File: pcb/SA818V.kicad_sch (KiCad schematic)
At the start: 7 parts, among them J12 RF_SMA, Q11 BSS138, Q12 BSS138, U19 SA818S-V

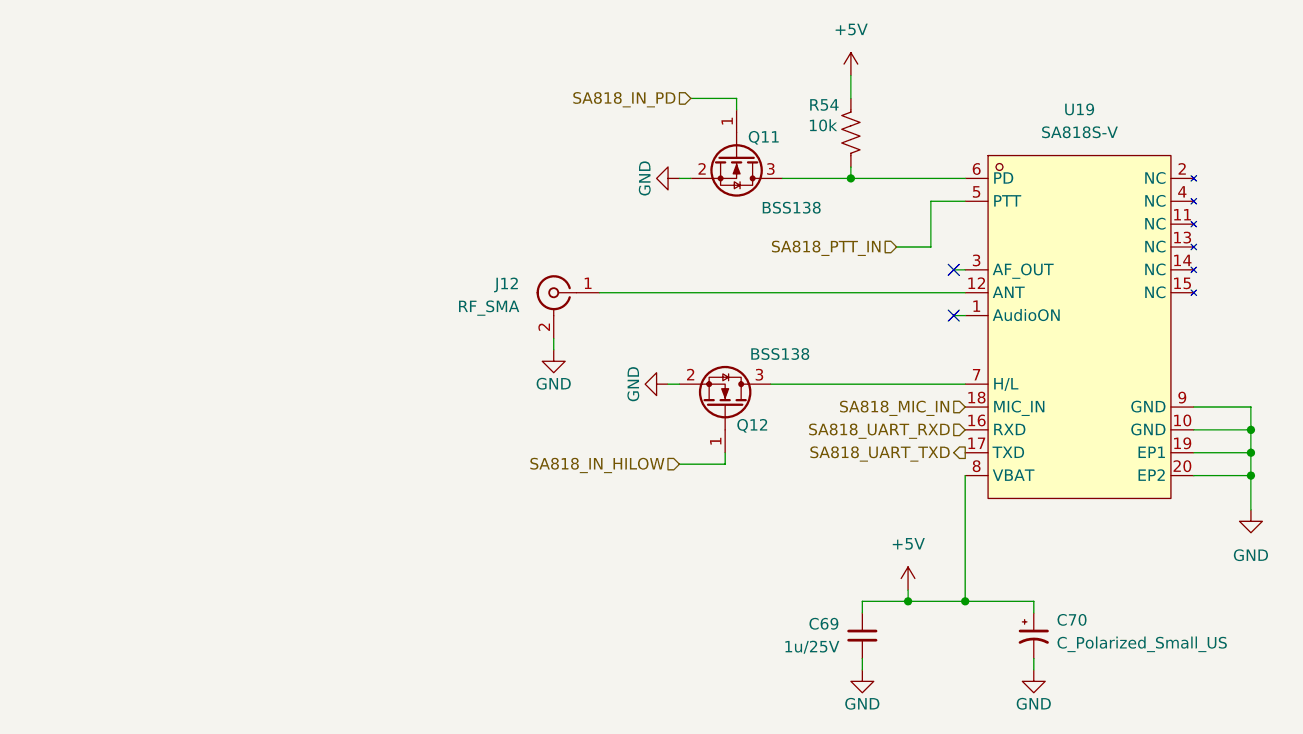
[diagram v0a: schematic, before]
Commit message: Wire SA818 PD/H-L and PTT opto, GPS power gating with bench bypass, RF detector groundwork
- SA818S-V: wire PD/H-L to PCA9555 expander outputs; swap PTT-keying FET
  for PC817 optocoupler isolation on the shared SA818S/external-HT PTT line
- GPS: add Q10 (AO3407A) high-side P-FET gating VCC+VCC_IO together for
  genuine hardware backup mode, driven via Q13 level-shifter from a new
  PCA9555 output (PERIPH_OUT_GPS_PWRON); add JP28 as a source-to-drain
  bench bypass across Q10 for unconditional power during bring-up; wire
  EXTINT to another PCA9555 output (PERIPH_OUT_GPS_EXTINT, pulled low by
  R57) to experiment with UART software-standby + external wake
- peripherals: reassign PCA9555 channels for the above plus SA818 PD/H-L
- audio/mcu-esp32: forward-power detector tap wiring groundwork
- docs: add vhf_matching_detector.md (matching network + RF detector BOM
  and layout), index it in _docs/README.md

Co-Authored-By: Claude Sonnet 5 <noreply@anthropic.com>
Claude-Session: https://claude.ai/code/session_01LhLkuH6sQ5GbUZ61bG7p2h
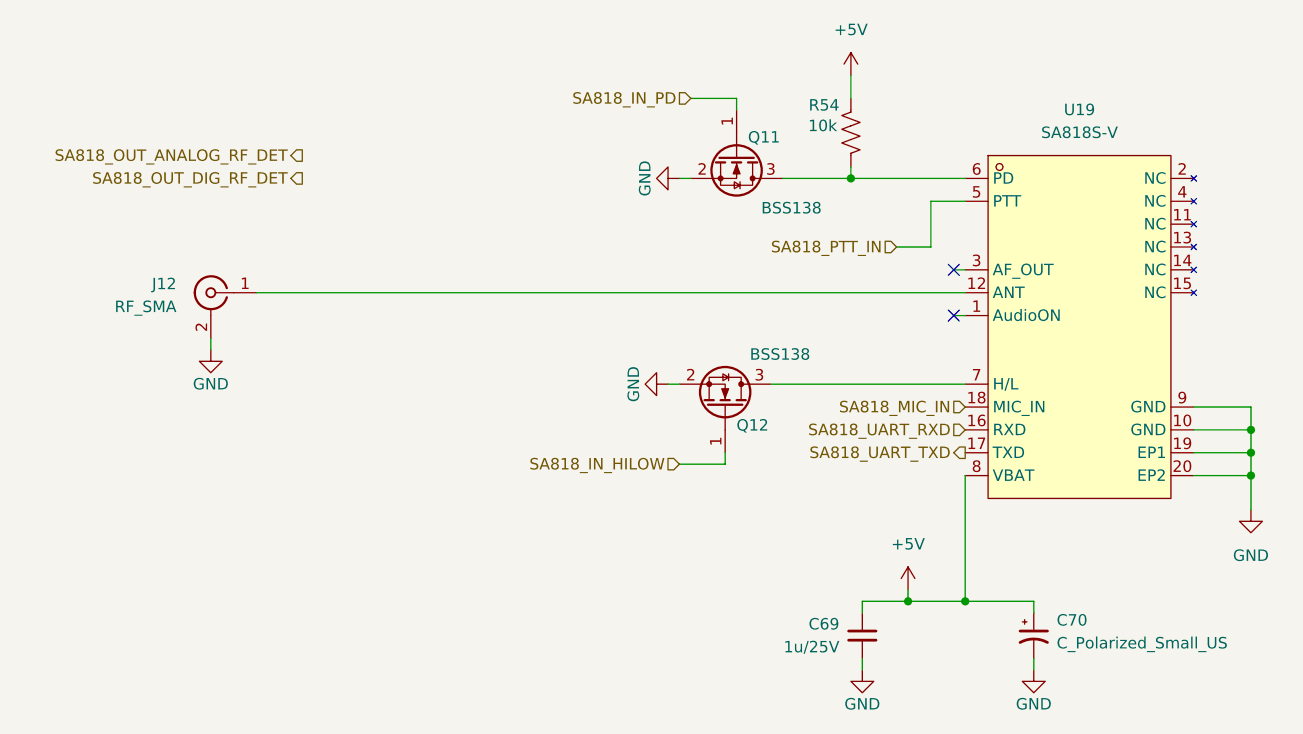
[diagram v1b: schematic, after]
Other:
- moved on the sheet: J12
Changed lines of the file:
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@@
 	(wire
 		(pts
-			(xy 82.55 80.01) (xy 82.55 81.28)
+			(xy 44.45 80.01) (xy 44.45 81.28)
 		)
 		(stroke
@@
 	(wire
 		(pts
-			(xy 87.63 74.93) (xy 128.27 74.93)
+			(xy 49.53 74.93) (xy 128.27 74.93)
 		)
 		(stroke
@@
 			(width 0)
 			(type default)
+		)
+	)
+	(hierarchical_label "SA818_OUT_ANALOG_RF_DET"
+		(shape output)
+		(at 54.61 59.69 180)
+		(effects
+			(font
+				(size 1.27 1.27)
+			)
+			(justify right)
 		)
 	)
@@
 		(shape input)
 		(at 120.65 69.85 180)
+		(effects
+			(font
+				(size 1.27 1.27)
+			)
+			(justify right)
+		)
+	)
+	(hierarchical_label "SA818_OUT_DIG_RF_DET"
+		(shape output)
+		(at 54.61 62.23 180)
 		(effects
 			(font
@@
 	(symbol
 		(lib_id "Connector:Conn_Coaxial")
-		(at 82.55 74.93 0)
+		(at 44.45 74.93 0)
 		(mirror y)
 		(unit 1)
@@
 		(dnp no)
 		(property "Reference" "J12"
-			(at 78.74 73.9531 0)
+			(at 40.64 73.9531 0)
 			(show_name no)
 			(do_not_autoplace no)
@@
 		)
 		(property "Value" "RF_SMA"
-			(at 78.74 76.4931 0)
+			(at 40.64 76.4931 0)
 			(show_name no)
 			(do_not_autoplace no)
@@
 		)
 		(property "Footprint" "Connector_Coaxial:SMA_Amphenol_132289_EdgeMount"
-			(at 82.55 74.93 0)
+			(at 44.45 74.93 0)
 			(hide yes)
 			(show_name no)
@@
 		)
 		(property "Datasheet" "https://www.lcsc.com/datasheet/C3174425.pdf"
-			(at 82.55 74.93 0)
+			(at 44.45 74.93 0)
 			(hide yes)
 			(show_name no)
@@
 		)
 		(property "Description" "CONN SMA 50Ω TH"
-			(at 82.55 74.93 0)
+			(at 44.45 74.93 0)
 			(hide yes)
 			(show_name no)
@@
 		)
 		(property "Manf" "Amphenol"
-			(at 82.55 74.93 0)
+			(at 44.45 74.93 0)
 			(hide yes)
 			(show_name no)
@@
 		)
 		(property "MPN" "132289"
-			(at 82.55 74.93 0)
+			(at 44.45 74.93 0)
 			(hide yes)
 			(show_name no)
@@
 		)
 		(property "LCSC Part #" "C3172723"
-			(at 82.55 74.93 0)
+			(at 44.45 74.93 0)
 			(hide yes)
 			(show_name no)
@@
 		)
 		(property "Package" "SMA"
-			(at 82.55 74.93 0)
+			(at 44.45 74.93 0)
 			(hide yes)
 			(show_name no)
@@
 	(symbol
 		(lib_id "PCM_SparkFun-PowerSymbol:GND")
-		(at 82.55 81.28 0)
+		(at 44.45 81.28 0)
 		(mirror y)
 		(unit 1)
@@
 		(fields_autoplaced yes)
 		(property "Reference" "#PWR0163"
-			(at 82.55 87.63 0)
+			(at 44.45 87.63 0)
 			(hide yes)
 			(show_name no)
@@
 		)
 		(property "Value" "GND"
-			(at 82.55 85.09 0)
+			(at 44.45 85.09 0)
 			(show_name no)
 			(do_not_autoplace yes)
@@
 		)
 		(property "Footprint" ""
-			(at 82.55 81.28 0)
+			(at 44.45 81.28 0)
 			(hide yes)
 			(show_name no)
@@
 		)
 		(property "Datasheet" ""
-			(at 82.55 81.28 0)
+			(at 44.45 81.28 0)
 			(hide yes)
 			(show_name no)
@@
 		)
 		(property "Description" "Power symbol creates a global label with name \"GND\" , ground"
-			(at 82.55 90.17 0)
-			(hide yes)
-			(show_name no)
+			(at 44.45 90.17 0)
+			(hide yes)
+			(show_name no)
